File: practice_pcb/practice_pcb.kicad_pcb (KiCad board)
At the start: 2 copper layers, 43.5 x 32.7 mm, 18 parts, among them J2 From_MCU, J3 MOSFET_out, J4 Conn_01x03, Q4 IRF3710, U5 NSi6651A

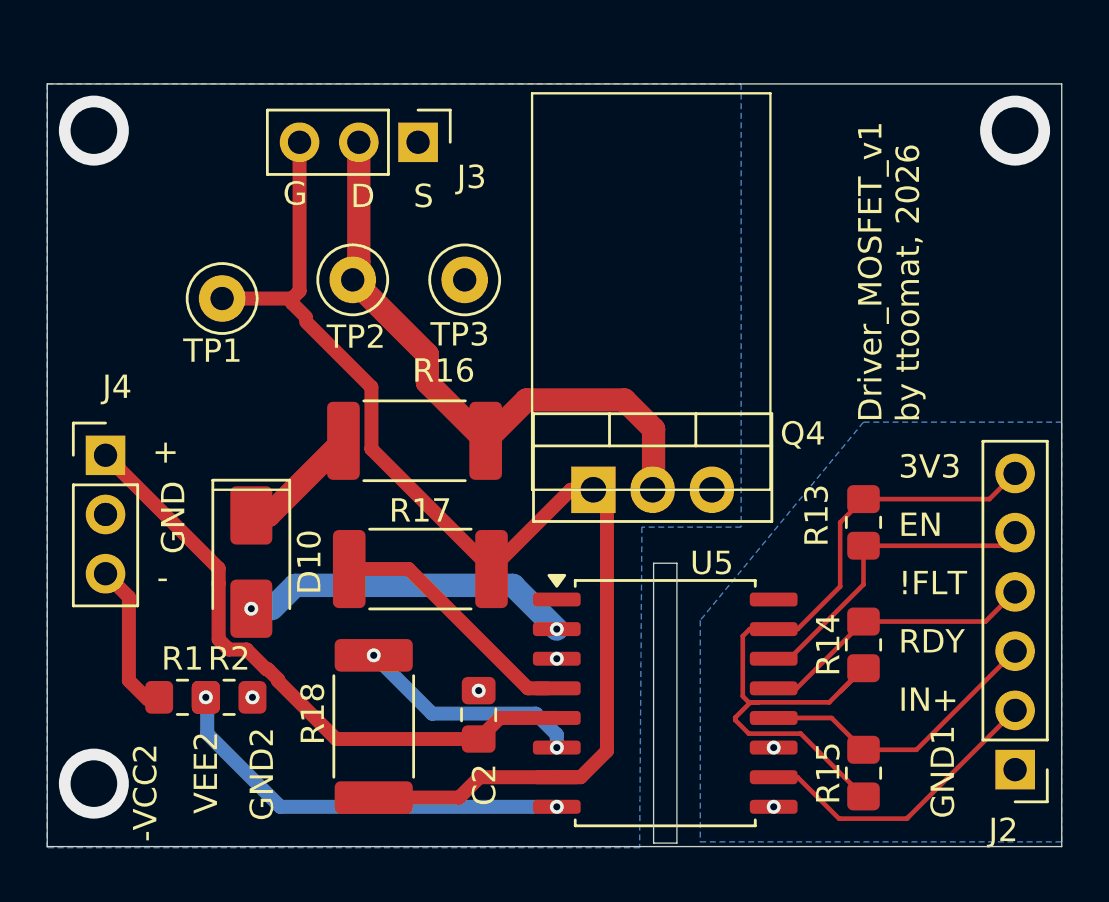
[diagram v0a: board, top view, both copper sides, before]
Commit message: PCB: non 45 wire angles.
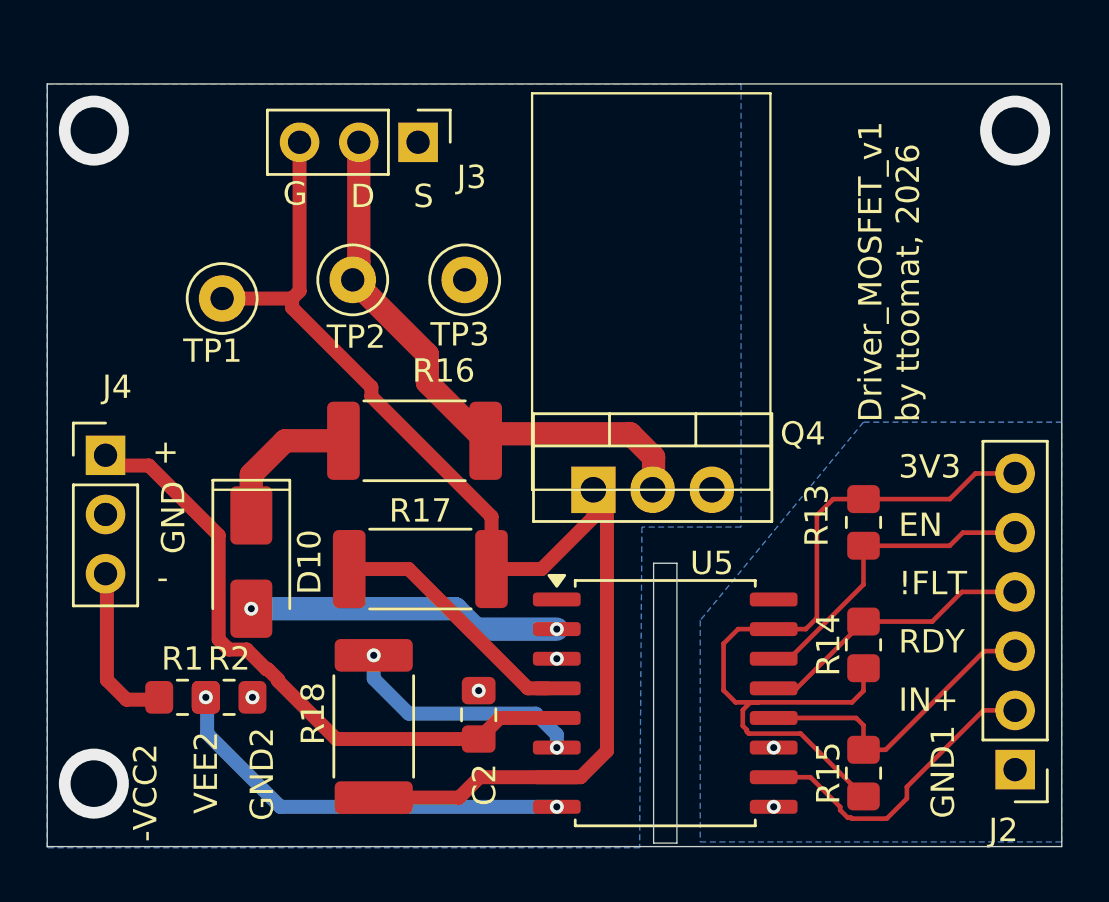
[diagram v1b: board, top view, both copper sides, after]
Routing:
- net drain: track 26.3 -> 24.4 mm
- net +3V3_DRV1: track 34.3 -> 35.5 mm
- net Net-(D10-K): track 5.74 -> 6.77 mm
- net gate: track 53.6 -> 54.5 mm
- net +15_DRV2: track 26.0 -> 26.8 mm
- net Net-(D10-A): track 14.3 -> 13.5 mm
- net Net-(J2-Pin_3): track 12.7 -> 13.3 mm
- net Net-(U5-OUTL): track 9.81 -> 10.4 mm
- net -15_DRV2: track 6.07 -> 6.61 mm
